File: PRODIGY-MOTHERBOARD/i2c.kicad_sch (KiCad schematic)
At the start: 0 parts

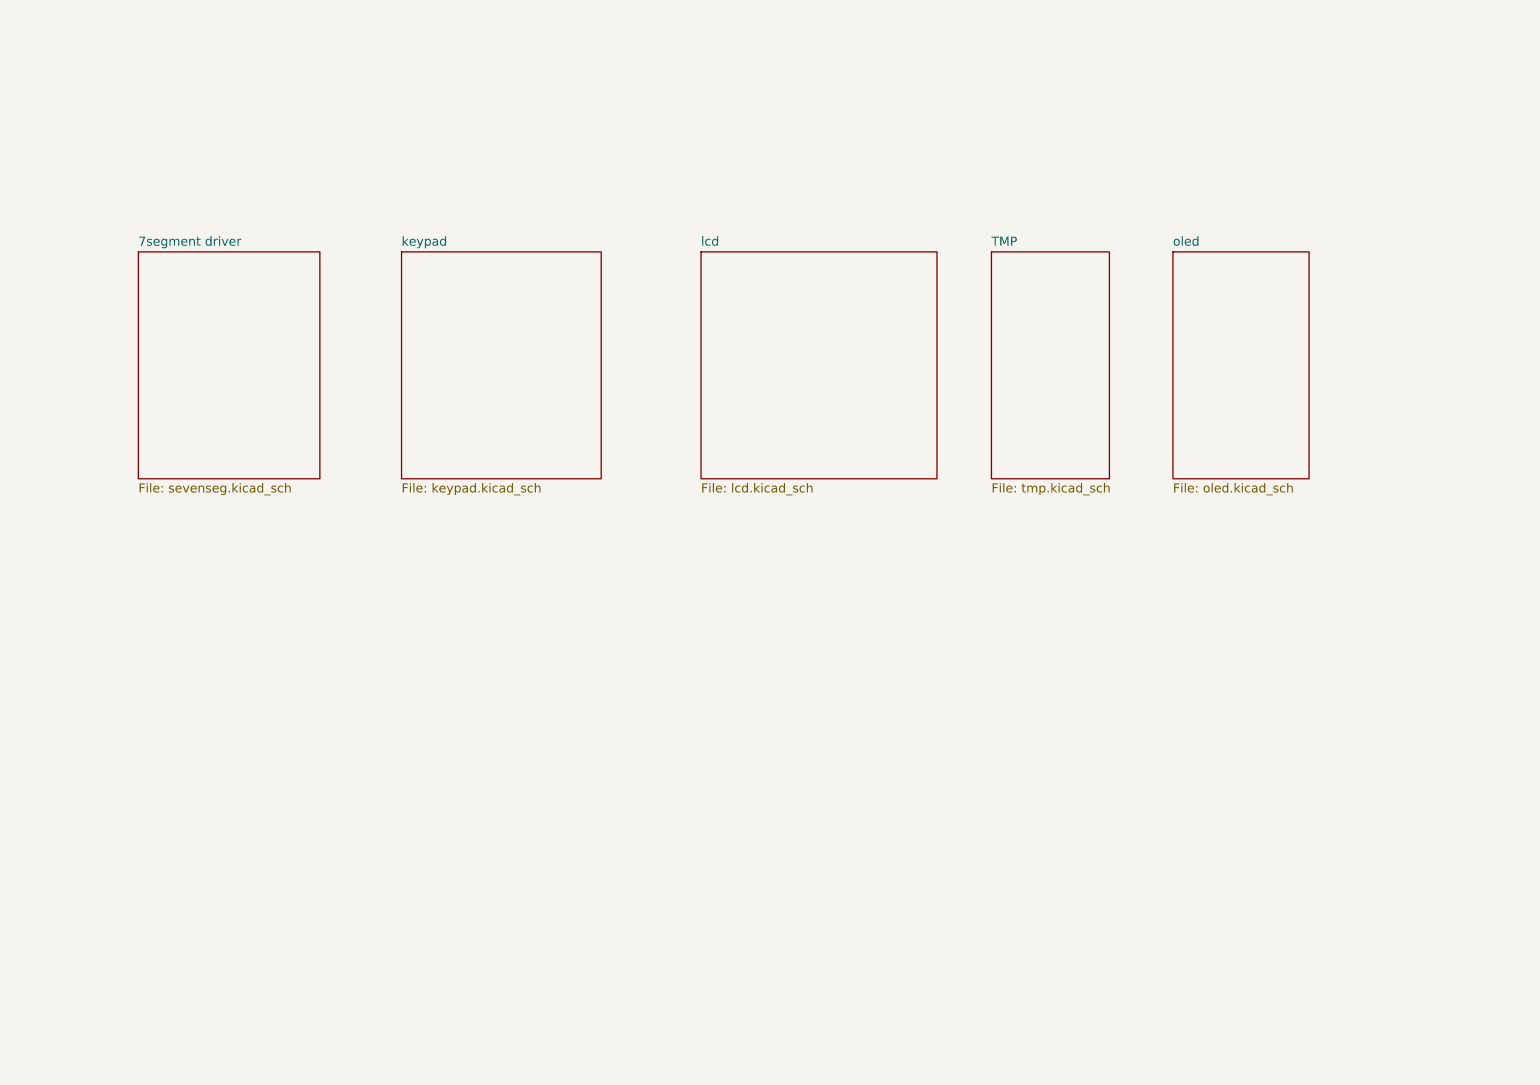
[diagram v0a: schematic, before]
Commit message: Finished I2C device and bus schematics. Added logic level translation.
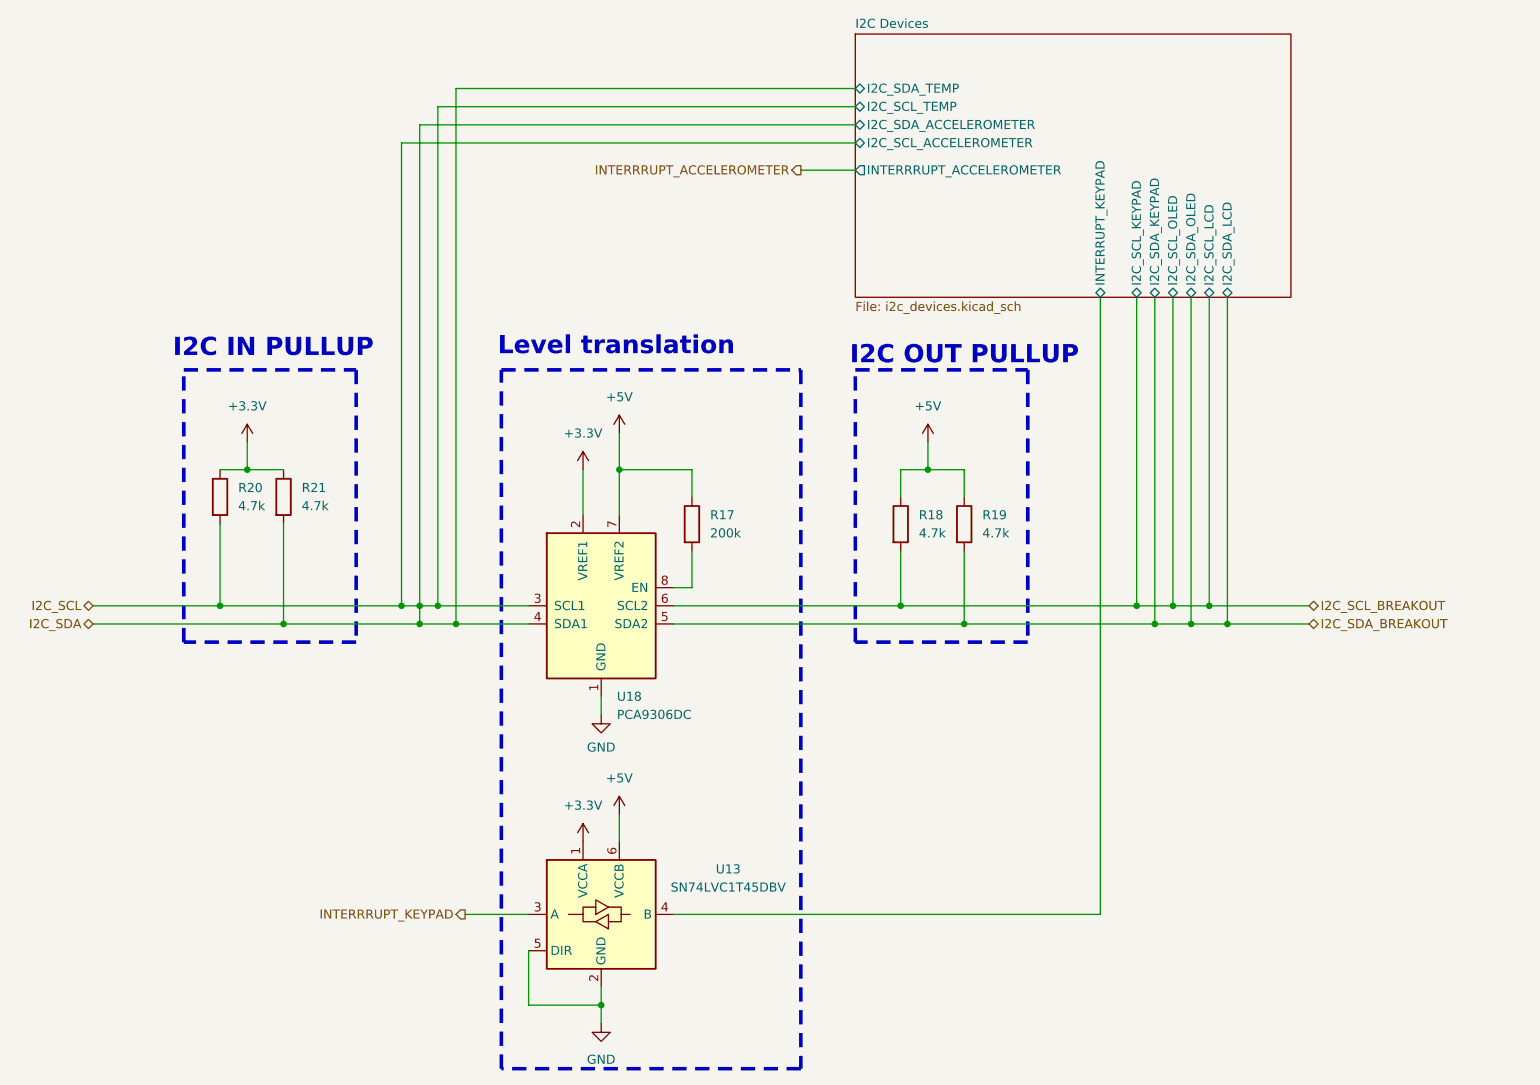
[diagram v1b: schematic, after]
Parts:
- added R17: 200k, symbol Device:R
- added R18, R19, R20, R21: 4.7k, symbol Device:R
- added U13: SN74LVC1T45DBV, Package_TO_SOT_SMD:SOT-23-6, symbol Logic_LevelTranslator:SN74LVC1T45DBV
- added U18: PCA9306DC, Package_SO:VSSOP-8_2.3x2mm_P0.5mm, symbol Interface:PCA9306DC
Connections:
- new net: R17.2, U18.8 (EN)
- new net +3.3V: R20.1, R21.1, U13.1 (VCCA), U18.2 (VREF1)
- new net +5V: R17.1, R18.1, R19.1, U13.6 (VCCB), U18.7 (VREF2)
- new net GND: U13.2 (GND), U13.5 (DIR), U18.1 (GND)
- new net I2C Devices/INTERRUPT_KEYPAD: U13.4 (B)
- new net I2C_SCL: R20.2, R21.2, U18.3 (SCL1), U18.4 (SDA1)
- new net I2C_SCL_BREAKOUT: R18.2, U18.6 (SCL2)
- new net I2C_SDA_BREAKOUT: R19.2, U18.5 (SDA2)
- new net INTERRRUPT_KEYPAD: U13.3 (A)
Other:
- removed sheet 7segment driver
- removed sheet TMP
- removed sheet keypad
- removed sheet lcd
- removed sheet oled
- added sheet I2C Devices (i2c_devices.kicad_sch)
- note added: "I2C IN PULLUP"
- note added: "I2C OUT PULLUP"
- note added: "Level translation"

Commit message: CAN schematic done
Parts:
- renumbered R20 to R25, R21 to R26, R17 to R27, R18 to R28, R19 to R29, U18 to U13, U13 to U14
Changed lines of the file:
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@@
 		(dnp no)
 		(fields_autoplaced yes)
-		(property "Reference" "U13"
+		(property "Reference" "U14"
 			(at 148.59 143.5414 0)
 			(effects
@@
 			(project "PRODIGY-MOTHERBOARD"
 				(path "/f1c25860-8989-4190-bd24-2491d23ca7d9/68745e9f-546d-4e12-ac2b-ba23aeab0093"
-					(reference "U13")
+					(reference "U14")
 					(unit 1)
 				)
@@
 		(dnp no)
 		(fields_autoplaced yes)
-		(property "Reference" "U18"
+		(property "Reference" "U13"
 			(at 133.0041 119.38 0)
 			(effects
@@
 			(project "PRODIGY-MOTHERBOARD"
 				(path "/f1c25860-8989-4190-bd24-2491d23ca7d9/68745e9f-546d-4e12-ac2b-ba23aeab0093"
-					(reference "U18")
+					(reference "U13")
 					(unit 1)
 				)
@@
 		(dnp no)
 		(fields_autoplaced yes)
-		(property "Reference" "R19"
+		(property "Reference" "R29"
 			(at 184.15 93.9799 0)
 			(effects
@@
 			(project "PRODIGY-MOTHERBOARD"
 				(path "/f1c25860-8989-4190-bd24-2491d23ca7d9/68745e9f-546d-4e12-ac2b-ba23aeab0093"
-					(reference "R19")
+					(reference "R29")
 					(unit 1)
 				)
@@
 		(dnp no)
 		(fields_autoplaced yes)
-		(property "Reference" "#PWR044"
+		(property "Reference" "#PWR057"
 			(at 133.35 86.36 0)
 			(effects
@@
 			(project "PRODIGY-MOTHERBOARD"
 				(path "/f1c25860-8989-4190-bd24-2491d23ca7d9/68745e9f-546d-4e12-ac2b-ba23aeab0093"
-					(reference "#PWR044")
+					(reference "#PWR057")
 					(unit 1)
 				)
@@
 		(dnp no)
 		(fields_autoplaced yes)
-		(property "Reference" "R21"
+		(property "Reference" "R26"
 			(at 88.9 90.1699 0)
 			(effects
@@
 			(project "PRODIGY-MOTHERBOARD"
 				(path "/f1c25860-8989-4190-bd24-2491d23ca7d9/68745e9f-546d-4e12-ac2b-ba23aeab0093"
-					(reference "R21")
+					(reference "R26")
 					(unit 1)
 				)
@@
 		(dnp no)
 		(fields_autoplaced yes)
-		(property "Reference" "#PWR045"
+		(property "Reference" "#PWR053"
 			(at 128.27 91.44 0)
 			(effects
@@
 			(project "PRODIGY-MOTHERBOARD"
 				(path "/f1c25860-8989-4190-bd24-2491d23ca7d9/68745e9f-546d-4e12-ac2b-ba23aeab0093"
-					(reference "#PWR045")
+					(reference "#PWR053")
 					(unit 1)
 				)
@@
 		(dnp no)
 		(fields_autoplaced yes)
-		(property "Reference" "#PWR072"
+		(property "Reference" "#PWR059"
 			(at 176.53 87.63 0)
 			(effects
@@
 			(project "PRODIGY-MOTHERBOARD"
 				(path "/f1c25860-8989-4190-bd24-2491d23ca7d9/68745e9f-546d-4e12-ac2b-ba23aeab0093"
-					(reference "#PWR072")
+					(reference "#PWR059")
 					(unit 1)
 				)
@@
 		(dnp no)
 		(fields_autoplaced yes)
-		(property "Reference" "#PWR057"
+		(property "Reference" "#PWR052"
 			(at 81.28 87.63 0)
 			(effects
@@
 			(project "PRODIGY-MOTHERBOARD"
 				(path "/f1c25860-8989-4190-bd24-2491d23ca7d9/68745e9f-546d-4e12-ac2b-ba23aeab0093"
-					(reference "#PWR057")
+					(reference "#PWR052")
 					(unit 1)
 				)
@@
 		(on_board yes)
 		(dnp no)
-		(property "Reference" "#PWR043"
+		(property "Reference" "#PWR055"
 			(at 130.81 128.27 0)
 			(effects
@@
 			(project "PRODIGY-MOTHERBOARD"
 				(path "/f1c25860-8989-4190-bd24-2491d23ca7d9/68745e9f-546d-4e12-ac2b-ba23aeab0093"
-					(reference "#PWR043")
+					(reference "#PWR055")
 					(unit 1)
 				)
@@
 		(dnp no)
 		(fields_autoplaced yes)
-		(property "Reference" "#PWR054"
+		(property "Reference" "#PWR056"
 			(at 130.81 171.45 0)
 			(effects
@@
 			(project "PRODIGY-MOTHERBOARD"
 				(path "/f1c25860-8989-4190-bd24-2491d23ca7d9/68745e9f-546d-4e12-ac2b-ba23aeab0093"
-					(reference "#PWR054")
+					(reference "#PWR056")
 					(unit 1)
 				)
@@
 		(dnp no)
 		(fields_autoplaced yes)
-		(property "Reference" "R18"
+		(property "Reference" "R28"
 			(at 175.26 93.9799 0)
 			(effects
@@
 			(project "PRODIGY-MOTHERBOARD"
 				(path "/f1c25860-8989-4190-bd24-2491d23ca7d9/68745e9f-546d-4e12-ac2b-ba23aeab0093"
-					(reference "R18")
+					(reference "R28")
 					(unit 1)
 				)
@@
 		(dnp no)
 		(fields_autoplaced yes)
-		(property "Reference" "#PWR055"
+		(property "Reference" "#PWR058"
 			(at 133.35 139.7 0)
 			(effects
@@
 			(project "PRODIGY-MOTHERBOARD"
 				(path "/f1c25860-8989-4190-bd24-2491d23ca7d9/68745e9f-546d-4e12-ac2b-ba23aeab0093"
-					(reference "#PWR055")
+					(reference "#PWR058")
 					(unit 1)
 				)
@@
 		(dnp no)
 		(fields_autoplaced yes)
-		(property "Reference" "#PWR056"
+		(property "Reference" "#PWR054"
 			(at 128.27 143.51 0)
 			(effects
@@
 			(project "PRODIGY-MOTHERBOARD"
 				(path "/f1c25860-8989-4190-bd24-2491d23ca7d9/68745e9f-546d-4e12-ac2b-ba23aeab0093"
-					(reference "#PWR056")
+					(reference "#PWR054")
 					(unit 1)
 				)
@@
 		(dnp no)
 		(fields_autoplaced yes)
-		(property "Reference" "R17"
+		(property "Reference" "R27"
 			(at 146.05 93.9799 0)
 			(effects
@@
 			(project "PRODIGY-MOTHERBOARD"
 				(path "/f1c25860-8989-4190-bd24-2491d23ca7d9/68745e9f-546d-4e12-ac2b-ba23aeab0093"
-					(reference "R17")
+					(reference "R27")
 					(unit 1)
 				)
@@
 		(dnp no)
 		(fields_autoplaced yes)
-		(property "Reference" "R20"
+		(property "Reference" "R25"
 			(at 80.01 90.1699 0)
 			(effects
@@
 			(project "PRODIGY-MOTHERBOARD"
 				(path "/f1c25860-8989-4190-bd24-2491d23ca7d9/68745e9f-546d-4e12-ac2b-ba23aeab0093"
-					(reference "R20")
-					(unit 1)
-				)
+					(reference "R25")
+					(unit 1)
+				)

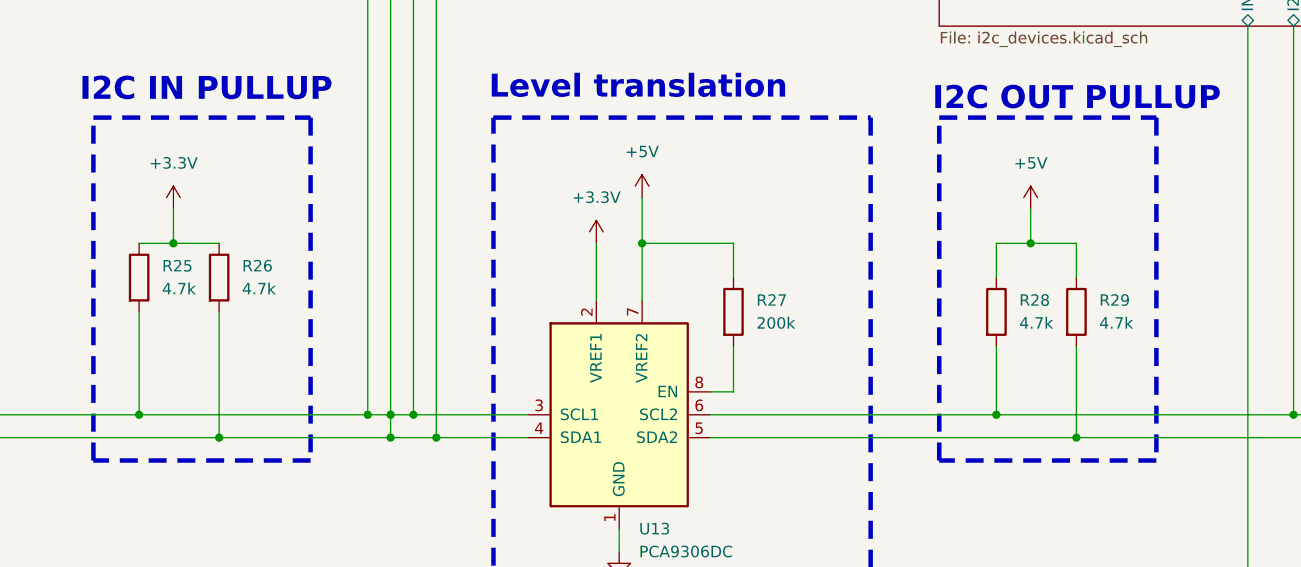
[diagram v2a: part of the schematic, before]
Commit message: SPI NFC schematic done.
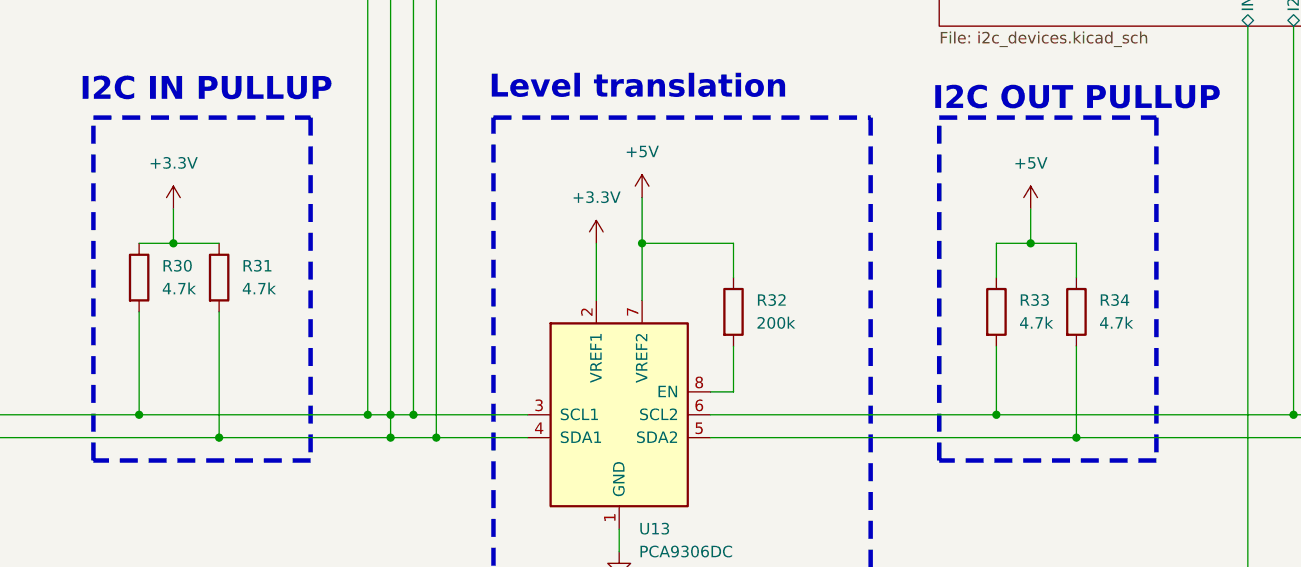
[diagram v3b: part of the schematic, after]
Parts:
- renumbered R25 to R30, R26 to R31, R27 to R32, R28 to R33, R29 to R34
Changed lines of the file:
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@@
 		(dnp no)
 		(fields_autoplaced yes)
-		(property "Reference" "R29"
+		(property "Reference" "R34"
 			(at 184.15 93.9799 0)
 			(effects
@@
 			(project "PRODIGY-MOTHERBOARD"
 				(path "/f1c25860-8989-4190-bd24-2491d23ca7d9/68745e9f-546d-4e12-ac2b-ba23aeab0093"
-					(reference "R29")
+					(reference "R34")
 					(unit 1)
 				)
@@
 		(dnp no)
 		(fields_autoplaced yes)
-		(property "Reference" "#PWR057"
+		(property "Reference" "#PWR076"
 			(at 133.35 86.36 0)
 			(effects
@@
 			(project "PRODIGY-MOTHERBOARD"
 				(path "/f1c25860-8989-4190-bd24-2491d23ca7d9/68745e9f-546d-4e12-ac2b-ba23aeab0093"
-					(reference "#PWR057")
+					(reference "#PWR076")
 					(unit 1)
 				)
@@
 		(dnp no)
 		(fields_autoplaced yes)
-		(property "Reference" "R26"
+		(property "Reference" "R31"
 			(at 88.9 90.1699 0)
 			(effects
@@
 			(project "PRODIGY-MOTHERBOARD"
 				(path "/f1c25860-8989-4190-bd24-2491d23ca7d9/68745e9f-546d-4e12-ac2b-ba23aeab0093"
-					(reference "R26")
+					(reference "R31")
 					(unit 1)
 				)
@@
 		(dnp no)
 		(fields_autoplaced yes)
-		(property "Reference" "#PWR053"
+		(property "Reference" "#PWR072"
 			(at 128.27 91.44 0)
 			(effects
@@
 			(project "PRODIGY-MOTHERBOARD"
 				(path "/f1c25860-8989-4190-bd24-2491d23ca7d9/68745e9f-546d-4e12-ac2b-ba23aeab0093"
-					(reference "#PWR053")
+					(reference "#PWR072")
 					(unit 1)
 				)
@@
 		(dnp no)
 		(fields_autoplaced yes)
-		(property "Reference" "#PWR059"
+		(property "Reference" "#PWR078"
 			(at 176.53 87.63 0)
 			(effects
@@
 			(project "PRODIGY-MOTHERBOARD"
 				(path "/f1c25860-8989-4190-bd24-2491d23ca7d9/68745e9f-546d-4e12-ac2b-ba23aeab0093"
-					(reference "#PWR059")
+					(reference "#PWR078")
 					(unit 1)
 				)
@@
 		(dnp no)
 		(fields_autoplaced yes)
-		(property "Reference" "#PWR052"
+		(property "Reference" "#PWR071"
 			(at 81.28 87.63 0)
 			(effects
@@
 			(project "PRODIGY-MOTHERBOARD"
 				(path "/f1c25860-8989-4190-bd24-2491d23ca7d9/68745e9f-546d-4e12-ac2b-ba23aeab0093"
-					(reference "#PWR052")
+					(reference "#PWR071")
 					(unit 1)
 				)
@@
 		(on_board yes)
 		(dnp no)
-		(property "Reference" "#PWR055"
+		(property "Reference" "#PWR074"
 			(at 130.81 128.27 0)
 			(effects
@@
 			(project "PRODIGY-MOTHERBOARD"
 				(path "/f1c25860-8989-4190-bd24-2491d23ca7d9/68745e9f-546d-4e12-ac2b-ba23aeab0093"
-					(reference "#PWR055")
+					(reference "#PWR074")
 					(unit 1)
 				)
@@
 		(dnp no)
 		(fields_autoplaced yes)
-		(property "Reference" "#PWR056"
+		(property "Reference" "#PWR075"
 			(at 130.81 171.45 0)
 			(effects
@@
 			(project "PRODIGY-MOTHERBOARD"
 				(path "/f1c25860-8989-4190-bd24-2491d23ca7d9/68745e9f-546d-4e12-ac2b-ba23aeab0093"
-					(reference "#PWR056")
+					(reference "#PWR075")
 					(unit 1)
 				)
@@
 		(dnp no)
 		(fields_autoplaced yes)
-		(property "Reference" "R28"
+		(property "Reference" "R33"
 			(at 175.26 93.9799 0)
 			(effects
@@
 			(project "PRODIGY-MOTHERBOARD"
 				(path "/f1c25860-8989-4190-bd24-2491d23ca7d9/68745e9f-546d-4e12-ac2b-ba23aeab0093"
-					(reference "R28")
+					(reference "R33")
 					(unit 1)
 				)
@@
 		(dnp no)
 		(fields_autoplaced yes)
-		(property "Reference" "#PWR058"
+		(property "Reference" "#PWR077"
 			(at 133.35 139.7 0)
 			(effects
@@
 			(project "PRODIGY-MOTHERBOARD"
 				(path "/f1c25860-8989-4190-bd24-2491d23ca7d9/68745e9f-546d-4e12-ac2b-ba23aeab0093"
-					(reference "#PWR058")
+					(reference "#PWR077")
 					(unit 1)
 				)
@@
 		(dnp no)
 		(fields_autoplaced yes)
-		(property "Reference" "#PWR054"
+		(property "Reference" "#PWR073"
 			(at 128.27 143.51 0)
 			(effects
@@
 			(project "PRODIGY-MOTHERBOARD"
 				(path "/f1c25860-8989-4190-bd24-2491d23ca7d9/68745e9f-546d-4e12-ac2b-ba23aeab0093"
-					(reference "#PWR054")
+					(reference "#PWR073")
 					(unit 1)
 				)
@@
 		(dnp no)
 		(fields_autoplaced yes)
-		(property "Reference" "R27"
+		(property "Reference" "R32"
 			(at 146.05 93.9799 0)
 			(effects
@@
 			(project "PRODIGY-MOTHERBOARD"
 				(path "/f1c25860-8989-4190-bd24-2491d23ca7d9/68745e9f-546d-4e12-ac2b-ba23aeab0093"
-					(reference "R27")
+					(reference "R32")
 					(unit 1)
 				)
@@
 		(dnp no)
 		(fields_autoplaced yes)
-		(property "Reference" "R25"
+		(property "Reference" "R30"
 			(at 80.01 90.1699 0)
 			(effects
@@
 			(project "PRODIGY-MOTHERBOARD"
 				(path "/f1c25860-8989-4190-bd24-2491d23ca7d9/68745e9f-546d-4e12-ac2b-ba23aeab0093"
-					(reference "R25")
-					(unit 1)
-				)
+					(reference "R30")
+					(unit 1)
+				)
